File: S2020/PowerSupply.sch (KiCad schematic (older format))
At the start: 25 parts, among them T1 4:1

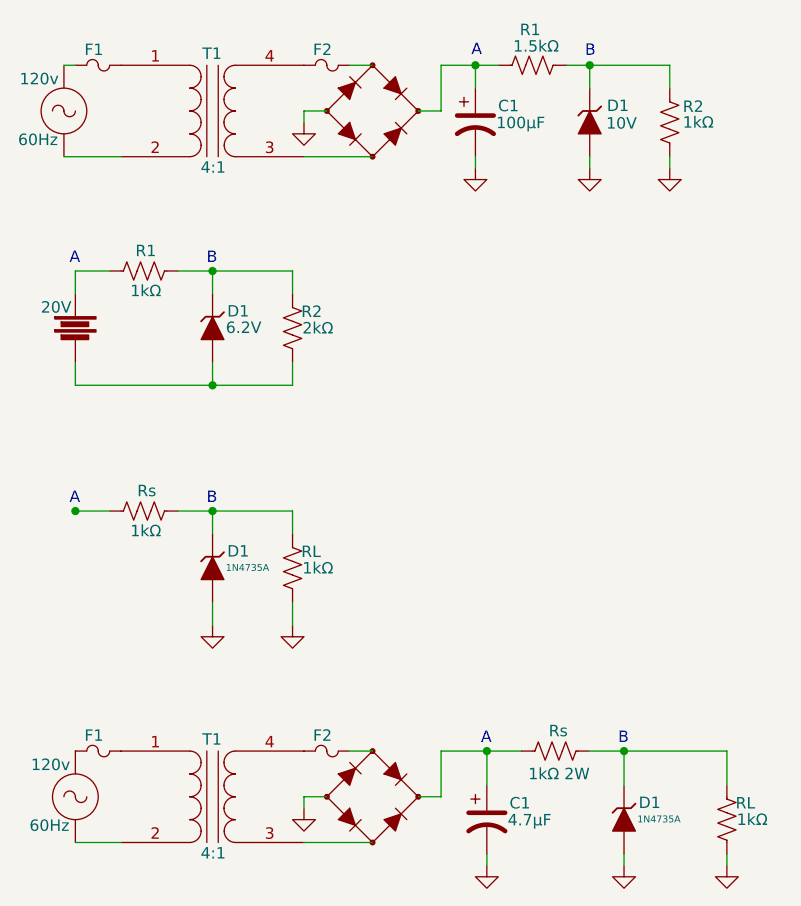
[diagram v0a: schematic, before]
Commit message: add limiters
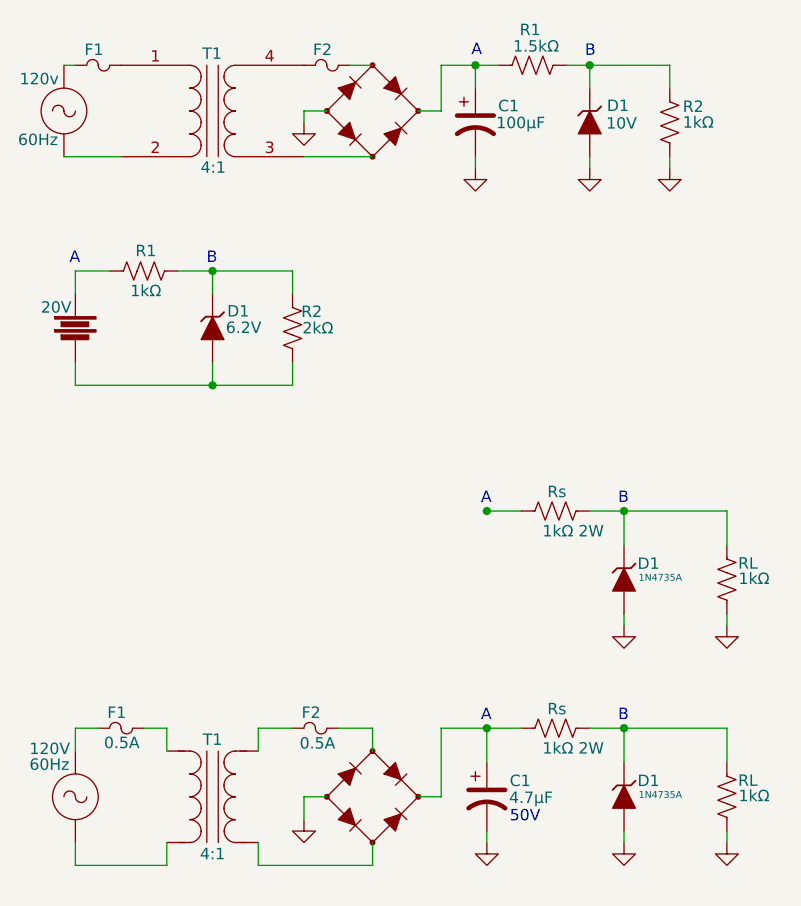
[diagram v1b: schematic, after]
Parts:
- removed T1: 4:1, symbol S2020-rescue:Transformer_1P_1S-sDevice
- added T1: 4:1, symbol 00TJR:Transformer
- 60Hz: value 120v -> 120V
- F1, F2: value Fuse1A -> 0.5A
- Rs: value 1kΩ -> 1kΩ 2W
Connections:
- net at F1.~: now also T1.1 (AA)
- net at 60Hz.2: now also T1.2 (AB)
- net at D?.2: now also T1.3 (SA)
- net at F2.~: now also T1.4 (SB)
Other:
- note added: "50V"
- moved on the sheet: C1, D1, F1, F2, RL, Rs

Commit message: save schematic
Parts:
- Rs: value 1kΩ 2W -> 1kΩ
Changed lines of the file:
@@
 P 3350 3200
 F 0 "Rs" V 3434 3152 50  0000 L CNN
-F 1 "1kΩ 2W" V 3262 2988 50  0000 L CNN
+F 1 "1kΩ" V 3263 3123 50  0000 L CNN
 F 2 "" V 3390 3190 50  0001 C CNN
 F 3 "~" H 3350 3200 50  0001 C CNN

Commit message: mess
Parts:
- removed D1: 1N4735A, symbol 00TJR:ZENER-RESCUE-F2018
- removed RL: 1kΩ, symbol S2020-rescue:R_US-sDevice
- added BT2, BT3: 0V-60V, symbol 00TJR:Battery-Variable
- added D5, D6: 1N4740A, symbol 00TJR:ZENER-RESCUE-F2018
- added RL1, Rs2: 1kΩ, symbol S2020-rescue:R_US-sDevice
- D7: renamed from D1; value 1N4735A -> 1N4740A
- gave numbers to parts that had none: 1
- renumbered 60Hz to 60Hz1, 60Hz to 60Hz2, C1 to C3, C1 to C4, D1 to D2, D1 to D4, F1 to F2, F2 to F3, F2 to F4, R1 to R10, R2 to R11, R1 to R8, R2 to R9, RL to RL2, Rs to Rs1, Rs to Rs3, T1 to T2
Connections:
- net GND: now also BT3.2, D6.2 (A), RL1.2
- net at Rs1.2: now also D5.1 (K)
- net at Rs1.1: now also BT2.1
- new net: BT2.2, D5.2 (A)
- new net: BT3.1, Rs2.1
- new net: D6.1 (K), RL1.1, Rs2.2
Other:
- moved on the sheet: Rs1
